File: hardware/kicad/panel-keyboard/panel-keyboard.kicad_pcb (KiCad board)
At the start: 2 copper layers, 100 x 150 mm, 117 parts, among them J2 PinHeader_1x04_P1.27mm_Vertic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, J485 2EDGVC-03P, Q12 SOT-23, SW1 Tact_12mm_THT, SW10 Tact_12mm_THT, SW11 Tact_12mm_THT, SW12 Tact_12mm_THT, SW13 Tact_12mm_THT, SW14 Tact_12mm_THT, SW15 Tact_12mm_THT, SW16 Tact_12mm_THT, SW2 Tact_12mm_THT, SW3 Tact_12mm_THT, SW4 Tact_12mm_THT, SW5 Tact_12mm_THT, SW6 Tact_12mm_THT, SW7 Tact_12mm_THT, SW8 Tact_12mm_THT, SW9 Tact_12mm_THT, U1 STM32F030F4P6, U2 TM1638, U3 SOIC-8_3.9x4.9mm_P1.27mm, U4 TO-263-5_TabPin3, U5 SOT-223-3_TabPin2

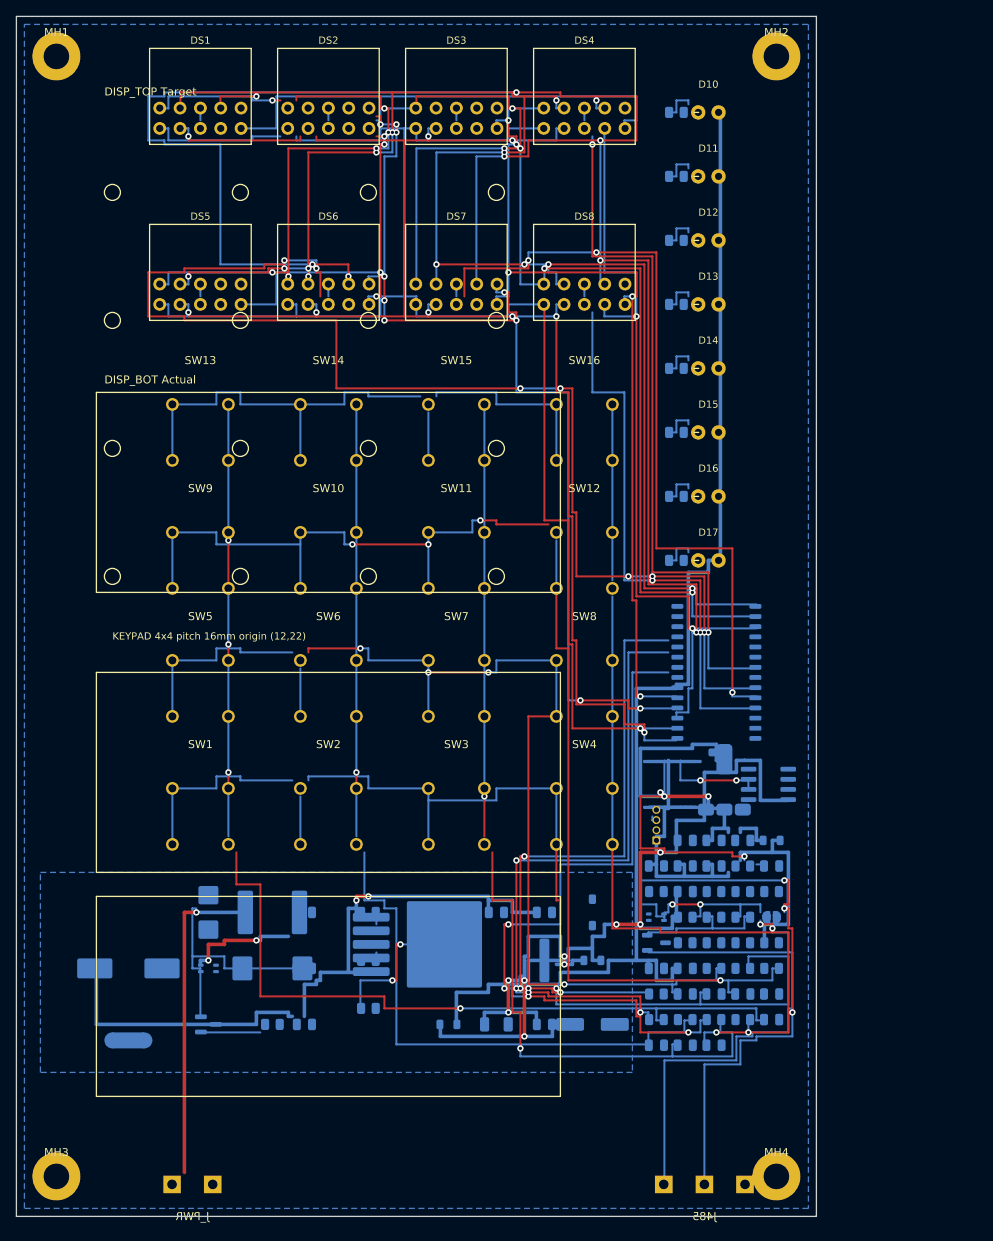
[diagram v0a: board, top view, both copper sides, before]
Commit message: update layout và chip để mạch thành dạng hình vuông 120x120mm
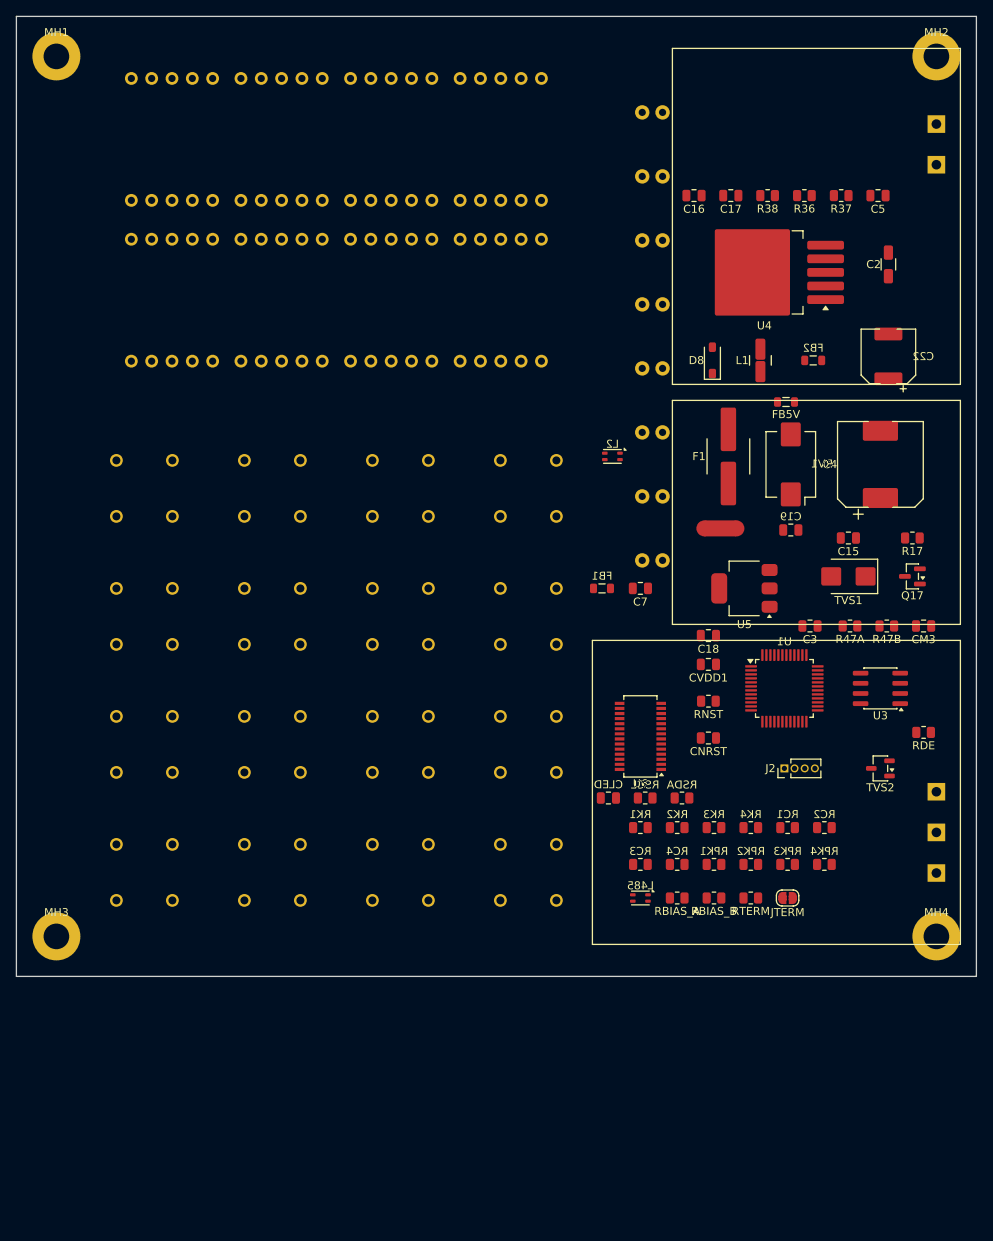
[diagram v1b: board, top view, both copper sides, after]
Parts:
- removed C14, CTM1, CTM2, CVDDA: C_0805_2012Metric, C_0805_2012Metric
- removed C21, CC1, CC2, CC3, CC4, CK1, CK2, CK3, CK4: C_0805_2012Metric, Capacitor_SMD:C_0805_2012Metric
- removed Q12: SOT-23, SOT-23
- removed R33A, R33B, R33C, RBOT0, RLED1, RLED2, RLED3, RLED4, RLED5, RLED6, RLED7, RLED8, RPU: R_0805_2012Metric, R_0805_2012Metric
- removed U2: TM1638, Panel:SOIC-28_TM1638
- added CLED: 100n, Capacitor_SMD:C_0805_2012Metric, F.Cu at (74.0, 97.7)
- added Q17: AO4407A, SOT-23, F.Cu at (112.0, 70.0)
- added RPK1: 10k, Resistor_SMD:R_0805_2012Metric, F.Cu at (87.2, 106.0)
- added RPK2: 10k, Resistor_SMD:R_0805_2012Metric, F.Cu at (91.8, 106.0)
- added RPK3: 10k, Resistor_SMD:R_0805_2012Metric, F.Cu at (96.4, 106.0)
- added RPK4: 10k, Resistor_SMD:R_0805_2012Metric, F.Cu at (101.0, 106.0)
- added RSCL: R_0805_2012Metric, Resistor_SMD:R_0805_2012Metric, F.Cu at (78.6, 97.7)
- added RSDA: R_0805_2012Metric, Resistor_SMD:R_0805_2012Metric, F.Cu at (83.2, 97.7)
- added U6: HT16K33A, HT16K33A_SSOP28, F.Cu at (78.0, 90.0)
- C15, C16, C17, C18, C19, C2, C22, C3, C4, C5, C7, CM3, CNRST, CVDD1, D8, F1, FB1, FB2, FB5V, J2, J485, JTERM, J_PWR, L1, L2, L485, NT1, R17, R36, R37, R38, R47A, R47B, RBIAS_A, RBIAS_B, RC1, RC2, RC3, RC4, RDE, RK1, RK2, RK3, RK4, RNST, RTERM, RV1, TVS1, TVS2, U3, U4, U5: moved to F.Cu
- D10, D11, D12, D13, D14, D15, D16, D17, DS1, DS2, DS3, DS4, DS5, DS6, DS7, DS8, SW1, SW10, SW11, SW12, SW13, SW14, SW15, SW16, SW2, SW3, SW4, SW5, SW6, SW7, SW8, SW9: moved to B.Cu
- U1: value STM32F030F4P6 -> STM32G030C8T6; footprint TSSOP-20_4.4x6.5mm_P0.65mm -> LQFP-48_7x7mm_P0.5mm; moved to F.Cu
- moved J_PWR 159.8 mm to (115.0, 16.0), turned to 90 degrees
- moved R37 117.5 mm to (103.1, 22.4), turned to 180 degrees
- moved C4 113.2 mm to (108.0, 56.0), turned to 90 degrees
- moved C5 111.7 mm to (107.7, 22.4), turned to 180 degrees
- moved R36 110.0 mm to (98.5, 22.4), turned to 180 degrees
- moved C2 106.9 mm to (109.0, 31.0), turned to 90 degrees
- moved R38 102.6 mm to (93.9, 22.4), turned to 180 degrees
- moved R17 100.5 mm to (112.0, 65.2), turned to 180 degrees
- moved NT1 97.8 mm to (88.0, 64.0), turned to 180 degrees
- moved U4 93.7 mm to (93.5, 32.0), turned to 180 degrees
- moved C16 92.9 mm to (84.7, 22.4), turned to 180 degrees
- moved C17 92.6 mm to (89.3, 22.4), turned to 180 degrees
- moved C22 91.3 mm to (109.0, 42.5), turned to 90 degrees
- moved RV1 90.4 mm to (96.8, 56.0), turned to 90 degrees
- moved TVS1 90.4 mm to (104.0, 70.0), turned to 180 degrees
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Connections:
- D10 pad A: +5V_LED -> LED_ROW
- D10 pad K: STAT_LED_1 -> GRID_1
- D11 pad A: +5V_LED -> LED_ROW
- D11 pad K: STAT_LED_2 -> GRID_2
- D12 pad A: +5V_LED -> LED_ROW
- D12 pad K: STAT_LED_3 -> GRID_3
- D13 pad A: +5V_LED -> LED_ROW
- D13 pad K: STAT_LED_4 -> GRID_4
- D14 pad A: +5V_LED -> LED_ROW
- D14 pad K: STAT_LED_5 -> GRID_5
- D15 pad A: +5V_LED -> LED_ROW
- D15 pad K: STAT_LED_6 -> GRID_6
- D16 pad A: +5V_LED -> LED_ROW
- D16 pad K: STAT_LED_7 -> GRID_7
- D17 pad A: +5V_LED -> LED_ROW
- D17 pad K: STAT_LED_8 -> GRID_8
- DS1 pad 3: GRID_TOP_1 -> GRID_1
- DS1 pad 8: GRID_TOP_1 -> GRID_1
- DS2 pad 3: GRID_TOP_2 -> GRID_2
- DS2 pad 8: GRID_TOP_2 -> GRID_2
- DS3 pad 3: GRID_TOP_3 -> GRID_3
- DS3 pad 8: GRID_TOP_3 -> GRID_3
- DS4 pad 3: GRID_TOP_4 -> GRID_4
- DS4 pad 8: GRID_TOP_4 -> GRID_4
- DS5 pad 3: GRID_BOT_1 -> GRID_5
- DS5 pad 8: GRID_BOT_1 -> GRID_5
- DS6 pad 3: GRID_BOT_2 -> GRID_6
- DS6 pad 8: GRID_BOT_2 -> GRID_6
- DS7 pad 3: GRID_BOT_3 -> GRID_7
- DS7 pad 8: GRID_BOT_3 -> GRID_7
- DS8 pad 3: GRID_BOT_4 -> GRID_8
- DS8 pad 8: GRID_BOT_4 -> GRID_8
- RC1 pad 1: TM_KS5 -> COL1
- RC2 pad 1: TM_KS6 -> COL2
- RC3 pad 1: TM_KS7 -> COL3
- RC4 pad 1: TM_KS8 -> COL4
- RK1 pad 1: TM_KS1 -> ROW1
- RK2 pad 1: TM_KS2 -> ROW2
- RK3 pad 1: TM_KS3 -> ROW3
- RK4 pad 1: TM_KS4 -> ROW4
- U1 pad 1: BOOT0 -> (no net)
- U1 pad 10: TM_CLK -> NRST
- U1 pad 11: TM_STB -> (no net)
- U1 pad 12: TM_DIO -> RS485_DE
- U1 pad 13: (no net) -> UART_TX
- U1 pad 14: (no net) -> UART_RX
- U1 pad 15: GND -> (no net)
- U1 pad 16: +3V3 -> (no net)
- U1 pad 19: SWDIO -> (no net)
- U1 pad 20: SWCLK -> (no net)
- U1 pad 4: NRST -> +3V3
- U1 pad 6: (no net) -> +3V3
- U1 pad 7: RS485_DE -> GND
- U1 pad 8: UART_TX -> (no net)
- U1 pad 9: UART_RX -> (no net)
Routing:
- net SEG6: track 253.0 -> 0.00 mm, vias 10 -> 0
- net SEG2: track 233.5 -> 0.00 mm, vias 12 -> 0
- net SEG1: track 226.0 -> 0.00 mm, vias 13 -> 0
- net SEG8: track 217.0 -> 0.00 mm, vias 9 -> 0
- net SEG5: track 202.0 -> 0.00 mm, vias 2 -> 0
- net SEG4: track 198.5 -> 0.00 mm, vias 9 -> 0
- net KEY_R2: track 165.0 -> 0.00 mm, vias 5 -> 0
- net KEY_R3: track 160.0 -> 0.00 mm, vias 5 -> 0
- net GRID_BOT_2: track 157.0 -> 0.00 mm, vias 7 -> 0
- net +5V_LED: track 155.0 -> 0.00 mm
- net KEY_C1: track 143.5 -> 0.00 mm, vias 7 -> 0
- net SEG7: track 124.5 -> 0.00 mm, vias 10 -> 0
- net KEY_C2: track 122.0 -> 0.00 mm, vias 2 -> 0
- net KEY_R1: track 120.0 -> 0.00 mm, vias 2 -> 0
- net KEY_C3: track 117.5 -> 0.00 mm, vias 2 -> 0
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- removed copper zone on B.Cu, net GND
- removed copper zone on B.Cu, net GND_PWR
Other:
- board size 100 x 150 mm -> 120 x 120 mm
- board text removed: "+24V"
- board text removed: "0V"
- board text removed: "A"
- board text removed: "B"
- board text removed: "Bottom edge: J_PWR (left) + J485 (right), gap >= 45 mm EMC"
- board text removed: "CNC opening 85x135 mm (centered)"
- board text removed: "DAY BO: 24V + buck + STM32"
- board text removed: "DISP_BOT Actual"
- board text removed: "DISP_TOP Target"
- board text removed: "Decal text zones (no copper)"
- board text removed: "J485 2EDG-5.08-03P A B SG"
- board text removed: "J_PWR 2P 5.08 +24V GND"
- board text removed: "KEYPAD 4x4 pitch 16mm origin (12,22)"
- board text removed: "Keypad Y center 46mm | LED column centered on keypad"
- board text removed: "Nguồn 24V"
- board text removed: "RS485"
- board text removed: "TOP ONLY: 4x4 switches, 2x 7-seg, 8x LED 0805 | BOTTOM: all IC/SMD"

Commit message: sửa danh sách linh kiện theo hương thương mại và add firmware cơ bản cho modbus
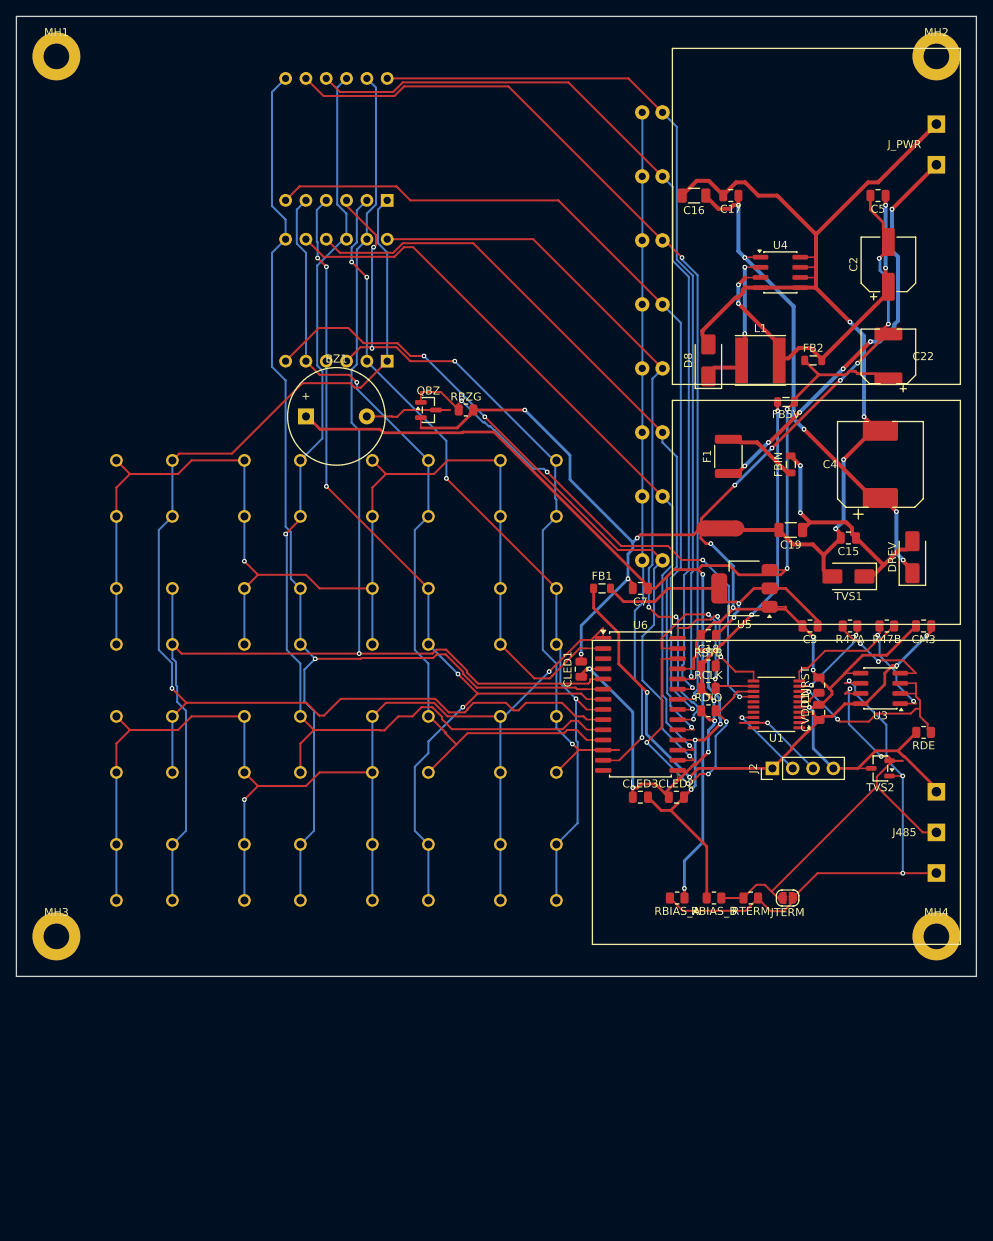
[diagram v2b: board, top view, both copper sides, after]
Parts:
- removed CLED: 100n, Capacitor_SMD:C_0805_2012Metric
- removed DS3, DS4, DS5, DS6, DS7, DS8: 0.56_CC, LED7seg_1digit_0.56in_CC_THT
- removed L2, L485: L_CommonModeChoke_Coilank_ACM2012, Inductor_SMD:L_CommonModeChoke_Coilank_ACM2012
- removed Q17: AO4407A, SOT-23
- removed R17, R36, R37, R38, RNST: R_0805_2012Metric, R_0805_2012Metric
- removed RC1, RC2, RC3, RC4, RK1, RK2, RK3, RK4, RSCL, RSDA: R_0805_2012Metric, Resistor_SMD:R_0805_2012Metric
- removed RPK1, RPK2, RPK3, RPK4: 10k, Resistor_SMD:R_0805_2012Metric
- removed RV1: Varistor_Panasonic_VF, Varistor:Varistor_Panasonic_VF
- added BZ1: Active buzzer 5V 12x9.5, Buzzer_12x9.5RM7.6, F.Cu at (36.2, 50.0)
- added CLED1: 100nF, C_0805_2012Metric, F.Cu at (70.6, 81.6)
- added CLED2: 100nF, C_0805_2012Metric, F.Cu at (82.5, 97.6)
- added CLED3: 10uF, C_0805_2012Metric, F.Cu at (78.0, 97.6)
- added DREV: SS34, D_SMA, F.Cu at (112.0, 67.6)
- added FBIN: 600R@100MHz 2A, L_0805_2012Metric, F.Cu at (96.8, 56.0)
- added QBZ: 2N7002, SOT-23, F.Cu at (51.5, 49.2)
- added RBZG: 100k, R_0805_2012Metric, F.Cu at (56.2, 49.2)
- added RCLK: 4.7k, R_0805_2012Metric, F.Cu at (86.5, 84.0)
- added RDIO: 4.7k, R_0805_2012Metric, F.Cu at (86.5, 86.8)
- added RSTB: 4.7k, R_0805_2012Metric, F.Cu at (86.5, 81.2)
- C15, C17: value C_0805_2012Metric -> 100nF 50V
- C16: value C_0805_2012Metric -> 10uF 50V; footprint C_0805_2012Metric -> C_1206_3216Metric
- C18, C5, CM3, CNRST, CVDD1: value C_0805_2012Metric -> 100nF
- C19: value C_0805_2012Metric -> 10uF 50V; footprint Capacitor_SMD:C_0805_2012Metric -> C_1206_3216Metric
- C2: value C_1206_3216Metric -> 220uF 10V; footprint C_1206_3216Metric -> CP_Elec_6.3x5.4
- C22: value CP_Elec_6.3x5.4 -> 220uF 10V
- C3: value C_0805_2012Metric -> 22uF
- C4: value CP_Elec_10x10.5 -> 470uF 35V
- C7: value C_0805_2012Metric -> 10uF
- D8: value D_SOD-123 -> SS34; footprint D_SOD-123 -> D_SMA
- DS1, DS2: value 0.56_CC -> 5641AS (4 digit 0.56in CC); footprint LED7seg_1digit_0.56in_CC_THT -> Display_4digit_0.56in_THT
- F1: value Fuse_2920_7451Metric -> PPTC 1812 0.5A 33V; footprint Fuse_2920_7451Metric -> Fuse_1812_4532Metric
- FB1, FB2, FB5V: value L_0805_2012Metric -> 120R@100MHz 2A
- J2: value PinHeader_1x04_P1.27mm_Vertical -> SWD (DNP); footprint PinHeader_1x04_P1.27mm_Vertical -> PinHeader_1x04_P2.54mm_Vertical
- J485: value 2EDGVC-03P -> KF2EDGV-5.08-3P
- JTERM: value SolderJumper-2_P1.3mm_Open_RoundedPad1.0x1.5mm -> 120R
- J_PWR: value 2EDGVC-02P -> KF2EDGV-5.08-2P
- L1: value L_1210_3225Metric -> 47uH 6045; footprint L_1210_3225Metric -> L_Taiyo-Yuden_NR-60xx
- NT1: value NetTie-2_SMD_Pad2.0mm -> GND_STAR
- R47A, R47B: value R_0805_2012Metric -> 47
- RBIAS_A, RBIAS_B: value R_0805_2012Metric -> 560
- RDE: value R_0805_2012Metric -> 10k
- RTERM: value R_0805_2012Metric -> 120
- SW1, SW10, SW11, SW12, SW13, SW14, SW15, SW16, SW2, SW3, SW4, SW5, SW6, SW7, SW8, SW9: value Tact_12mm_THT -> Tact_12mm
- TVS1: value D_SMB -> SMAJ28A; footprint D_SMB -> D_SMA
- TVS2: value SOT-23-3 -> SM712
- U1: value STM32G030C8T6 -> STM32G030F6P6; footprint LQFP-48_7x7mm_P0.5mm -> TSSOP-20_4.4x6.5mm_P0.65mm
- U3: value SOIC-8_3.9x4.9mm_P1.27mm -> SIT3485 / MAX3485
- U4: value TO-263-5_TabPin3 -> XL1509-5.0E1; footprint TO-263-5_TabPin3 -> SOIC-8_3.9x4.9mm_P1.27mm
- U5: value SOT-223-3_TabPin2 -> AMS1117-3.3
- U6: value HT16K33A -> TM1638; footprint HT16K33A_SSOP28 -> SOIC-28W_7.5x17.9mm_P1.27mm
- moved DS2 21.2 mm to (40.0, 35.5)
- moved DS1 20.6 mm to (40.0, 15.4)
- moved CNRST 15.3 mm to (100.3, 83.6), turned to 90 degrees
- moved CVDD1 15.0 mm to (100.3, 87.0), turned to 90 degrees
- moved U6 4.00 mm to (78.0, 86.0), turned to 0 degrees
- moved U1 2.24 mm to (95.0, 86.0)
- moved U4 2.00 mm to (95.5, 32.0), turned to 0 degrees
- moved J2 1.50 mm to (94.5, 94.0)
- moved D8 0.50 mm to (86.5, 43.0)
- turned L1 to 0 degrees
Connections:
- CM3 pad 1: +5V -> +3V3
- DS1 pad 10: SEG7 -> SEG6
- DS1 pad 3: GRID_1 -> SEG8
- DS1 pad 5: SEG8 -> SEG7
- DS1 pad 6: SEG2 -> GRID_4
- DS1 pad 7: SEG1 -> SEG2
- DS1 pad 8: GRID_1 -> GRID_3
- DS1 pad 9: SEG6 -> GRID_2
- DS2 pad 10: SEG7 -> SEG6
- DS2 pad 3: GRID_2 -> SEG8
- DS2 pad 5: SEG8 -> SEG7
- DS2 pad 6: SEG2 -> GRID_8
- DS2 pad 7: SEG1 -> SEG2
- DS2 pad 8: GRID_2 -> GRID_7
- DS2 pad 9: SEG6 -> GRID_6
- MH1 pad : GND -> (no net)
- MH2 pad : GND -> (no net)
- MH3 pad : GND -> (no net)
- MH4 pad : GND -> (no net)
- SW1 pad 1: KEY_R1 -> SEG1
- SW1 pad 2: KEY_C1 -> KEY_K1
- SW1 pad 3: KEY_C1 -> KEY_K1
- SW1 pad 4: KEY_R1 -> SEG1
- SW10 pad 1: KEY_R3 -> SEG2
- SW10 pad 2: KEY_C2 -> KEY_K2
- SW10 pad 3: KEY_C2 -> KEY_K2
- SW10 pad 4: KEY_R3 -> SEG2
- SW11 pad 1: KEY_R3 -> SEG3
- SW11 pad 2: KEY_C3 -> KEY_K2
- SW11 pad 3: KEY_C3 -> KEY_K2
- SW11 pad 4: KEY_R3 -> SEG3
- SW12 pad 1: KEY_R3 -> SEG4
- SW12 pad 2: KEY_C4 -> KEY_K2
- SW12 pad 3: KEY_C4 -> KEY_K2
- SW12 pad 4: KEY_R3 -> SEG4
- SW13 pad 1: KEY_R4 -> SEG5
- SW13 pad 2: KEY_C1 -> KEY_K2
- SW13 pad 3: KEY_C1 -> KEY_K2
- SW13 pad 4: KEY_R4 -> SEG5
- SW14 pad 1: KEY_R4 -> SEG6
- SW14 pad 2: KEY_C2 -> KEY_K2
- SW14 pad 3: KEY_C2 -> KEY_K2
- SW14 pad 4: KEY_R4 -> SEG6
- SW15 pad 1: KEY_R4 -> SEG7
- SW15 pad 2: KEY_C3 -> KEY_K2
- SW15 pad 3: KEY_C3 -> KEY_K2
- SW15 pad 4: KEY_R4 -> SEG7
- SW16 pad 1: KEY_R4 -> SEG8
- SW16 pad 2: KEY_C4 -> KEY_K2
- SW16 pad 3: KEY_C4 -> KEY_K2
- SW16 pad 4: KEY_R4 -> SEG8
- SW2 pad 1: KEY_R1 -> SEG2
- SW2 pad 2: KEY_C2 -> KEY_K1
- SW2 pad 3: KEY_C2 -> KEY_K1
- SW2 pad 4: KEY_R1 -> SEG2
- SW3 pad 1: KEY_R1 -> SEG3
- SW3 pad 2: KEY_C3 -> KEY_K1
- SW3 pad 3: KEY_C3 -> KEY_K1
- SW3 pad 4: KEY_R1 -> SEG3
- SW4 pad 1: KEY_R1 -> SEG4
- SW4 pad 2: KEY_C4 -> KEY_K1
- SW4 pad 3: KEY_C4 -> KEY_K1
- SW4 pad 4: KEY_R1 -> SEG4
- SW5 pad 1: KEY_R2 -> SEG5
- SW5 pad 2: KEY_C1 -> KEY_K1
- SW5 pad 3: KEY_C1 -> KEY_K1
- SW5 pad 4: KEY_R2 -> SEG5
- SW6 pad 1: KEY_R2 -> SEG6
- SW6 pad 2: KEY_C2 -> KEY_K1
- SW6 pad 3: KEY_C2 -> KEY_K1
- SW6 pad 4: KEY_R2 -> SEG6
- SW7 pad 1: KEY_R2 -> SEG7
- SW7 pad 2: KEY_C3 -> KEY_K1
- SW7 pad 3: KEY_C3 -> KEY_K1
- SW7 pad 4: KEY_R2 -> SEG7
- SW8 pad 1: KEY_R2 -> SEG8
- SW8 pad 2: KEY_C4 -> KEY_K1
- SW8 pad 3: KEY_C4 -> KEY_K1
- SW8 pad 4: KEY_R2 -> SEG8
- SW9 pad 1: KEY_R3 -> SEG1
- SW9 pad 2: KEY_C1 -> KEY_K2
- SW9 pad 3: KEY_C1 -> KEY_K2
- SW9 pad 4: KEY_R3 -> SEG1
- U1 pad 10: NRST -> UART_RX
- U1 pad 11: (no net) -> TM_STB
- U1 pad 12: RS485_DE -> TM_CLK
- U1 pad 13: UART_TX -> TM_DIO
- U1 pad 14: UART_RX -> BZ_ON
- U1 pad 18: (no net) -> SWDIO
- U1 pad 19: (no net) -> SWCLK
- U1 pad 5: +3V3 -> GND
- U1 pad 6: +3V3 -> NRST
- U1 pad 7: GND -> (no net)
- U1 pad 8: (no net) -> RS485_DE
- U1 pad 9: (no net) -> UART_TX
- U3 pad 6: RS485_A -> RS485_A_BUS
- U3 pad 7: RS485_B -> RS485_B_BUS
- U3 pad 8: +5V -> +3V3
- U4 pad 3: BUCK_FB -> +5V_RAW
- U4 pad 4: BUCK_EN -> GND_PWR
- U6 pad 1: GND -> KEY_K1
- U6 pad 10: (no net) -> SEG6
- U6 pad 11: (no net) -> SEG7
- U6 pad 12: (no net) -> SEG8
- U6 pad 13: (no net) -> LED_ROW
- U6 pad 15: (no net) -> +5V_LED
- U6 pad 16: (no net) -> GRID_8
- U6 pad 17: LED_ROW -> GRID_7
- U6 pad 18: SEG8 -> GND
- U6 pad 19: SEG7 -> GRID_6
- U6 pad 2: GRID_1 -> KEY_K2
- U6 pad 20: SEG6 -> GRID_5
- U6 pad 21: SEG5 -> GRID_4
- U6 pad 22: SEG4 -> GRID_3
- U6 pad 23: SEG3 -> GRID_2
- U6 pad 24: SEG2 -> GRID_1
- U6 pad 25: SEG1 -> GND
- U6 pad 26: SCL -> TM_DIO
- U6 pad 27: SDA -> TM_CLK
- U6 pad 28: +5V_LED -> TM_STB
- U6 pad 3: GRID_2 -> (no net)
- U6 pad 4: GRID_3 -> +5V_LED
- U6 pad 5: GRID_4 -> SEG1
- U6 pad 6: GRID_5 -> SEG2
- U6 pad 7: GRID_6 -> SEG3
- U6 pad 8: GRID_7 -> SEG4
- U6 pad 9: GRID_8 -> SEG5
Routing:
- net GND: track 0.00 -> 253.5 mm, vias 0 -> 19
- net SEG1: track 0.00 -> 171.3 mm, vias 0 -> 1
- net KEY_K1: track 0.00 -> 161.0 mm, vias 0 -> 2
- net KEY_K2: track 0.00 -> 157.4 mm, vias 0 -> 1
- net SEG5: track 0.00 -> 151.9 mm, vias 0 -> 1
- net +5V: track 0.00 -> 151.4 mm, vias 0 -> 4
- net SEG2: track 0.00 -> 147.1 mm, vias 0 -> 1
- net SEG6: track 0.00 -> 133.4 mm, vias 0 -> 1
- net GND_PWR: track 0.00 -> 126.3 mm, vias 0 -> 4
- net GRID_2: track 0.00 -> 116.6 mm, vias 0 -> 1
- net SEG3: track 0.00 -> 116.4 mm, vias 0 -> 5
- net GRID_3: track 0.00 -> 115.5 mm, vias 0 -> 2
- net GRID_1: track 0.00 -> 110.9 mm, vias 0 -> 1
- net GRID_4: track 0.00 -> 109.4 mm, vias 0 -> 1
- net SEG4: track 0.00 -> 105.1 mm, vias 0 -> 4
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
